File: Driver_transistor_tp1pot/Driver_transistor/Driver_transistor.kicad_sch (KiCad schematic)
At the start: 22 parts, among them J1 Conn_01x01, J2 Conn_01x03, Q1 BC557, Q2 BC548, Q3 BC548, Q4 BU208A

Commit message: actualizacion
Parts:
- added J6: Conn_01x01, Connector_PinHeader_2.00mm:PinHeader_1x01_P2.00mm_Vertical, symbol Connector_Generic:Conn_01x01
- Q4: footprint Package_TO_SOT_THT:TO-220-3_Vertical -> Package_TO_SOT_THT:TO-3
- R8: footprint Resistor_THT:R_Axial_DIN0207_L6.3mm_D2.5mm_P7.62mm_Horizontal -> Resistor_THT:R_Axial_Power_L20.0mm_W6.4mm_P22.40mm
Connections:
- net GND: now also Q4.1 (E), J6.1 (Pin_1); no longer Q4.3 (E)
- net at JP1.2 (B), R8.2: now also Q4.3 (C); no longer Q4.2 (C)
- net at D3.1 (K), JP2.2 (B): now also Q4.2 (B); no longer Q4.1 (B)
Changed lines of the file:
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@@
+    (stroke (width 0) (type default))
+  )
+  (wire (pts (xy 81.28 48.26) (xy 77.47 48.26))
+    (stroke (width 0) (type default))
+  )
+  (wire (pts (xy 77.47 48.26) (xy 77.47 50.8))
     (stroke (width 0) (type default))
   )
@@
     )
   )
+  (symbol (lib_id "Connector_Generic:Conn_01x01") (at 86.36 48.26 0) (unit 1)
+    (in_bom yes) (on_board yes) (dnp no) (fields_autoplaced)
+    (property "Reference" "J6" (at 88.9 47.625 0)
+      (effects (font (size 1.27 1.27)) (justify left))
+    )
+    (property "Value" "Conn_01x01" (at 88.9 50.165 0)
+      (effects (font (size 1.27 1.27)) (justify left))
+    )
+    (property "Footprint" "Connector_PinHeader_2.00mm:PinHeader_1x01_P2.00mm_Vertical" (at 86.36 48.26 0)
+      (effects (font (size 1.27 1.27)) hide)
+    )
+    (property "Datasheet" "~" (at 86.36 48.26 0)
+      (effects (font (size 1.27 1.27)) hide)
+    )
+    (pin "1")
+    (instances
+      (project "Driver_transistor"
+        (path "/e4287a4b-c4f2-447b-b63a-9e2c3468b7f7"
+          (reference "J6") (unit 1)
+        )
+      )
+    )
+  )
   (symbol (lib_id "Transistor_BJT:BUT11") (at 214.63 86.36 0) (unit 1)
     (in_bom yes) (on_board yes) (dnp no) (fields_autoplaced)
@@
       (effects (font (size 1.27 1.27)) (justify left))
     )
-    (property "Footprint" "Package_TO_SOT_THT:TO-220-3_Vertical" (at 219.71 88.265 0)
+    (property "Footprint" "Package_TO_SOT_THT:TO-3" (at 219.71 88.265 0)
       (effects (font (size 1.27 1.27) italic) (justify left) hide)
     )
@@
       (effects (font (size 1.27 1.27)) (justify left))
     )
-    (property "Footprint" "Resistor_THT:R_Axial_DIN0207_L6.3mm_D2.5mm_P7.62mm_Horizontal" (at 215.392 66.04 90)
+    (property "Footprint" "Resistor_THT:R_Axial_Power_L20.0mm_W6.4mm_P22.40mm" (at 215.392 66.04 90)
       (effects (font (size 1.27 1.27)) hide)
     )
@@
         )
       )
+    )
+  )
+  (symbol (lib_id "power:GND") (at 77.47 50.8 0) (unit 1)
+    (in_bom yes) (on_board yes) (dnp no) (fields_autoplaced)
+    (property "Reference" "#PWR019" (at 77.47 57.15 0)
+      (effects (font (size 1.27 1.27)) hide)
+    )
+    (property "Value" "GND" (at 77.47 55.88 0)
+      (effects (font (size 1.27 1.27)))
+    )
+    (property "Footprint" "" (at 77.47 50.8 0)
+      (effects (font (size 1.27 1.27)) hide)
+    )
+    (property "Datasheet" "" (at 77.47 50.8 0)
+      (effects (font (size 1.27 1.27)) hide)
+    )
+    (pin "1")
+    (instances
+      (project "Driver_transistor"
+        (path "/e4287a4b-c4f2-447b-b63a-9e2c3468b7f7"
+          (reference "#PWR019") (unit 1)
+        )
+      )

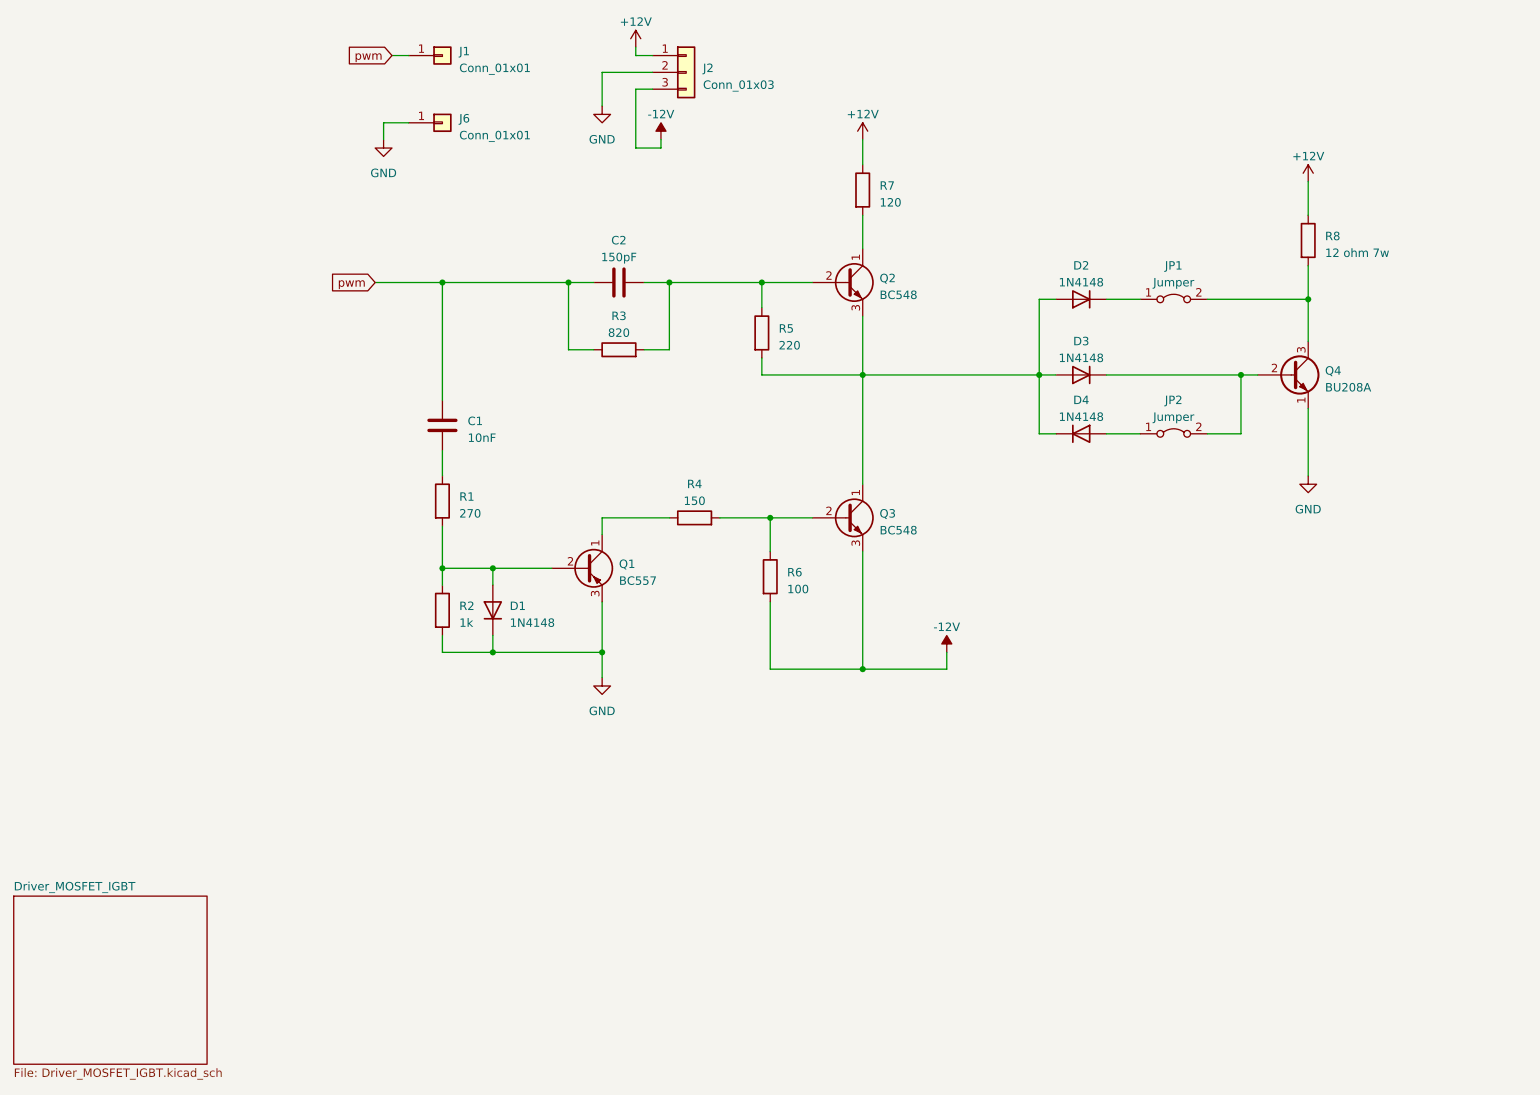
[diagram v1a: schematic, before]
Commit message: rediseño driver BJT
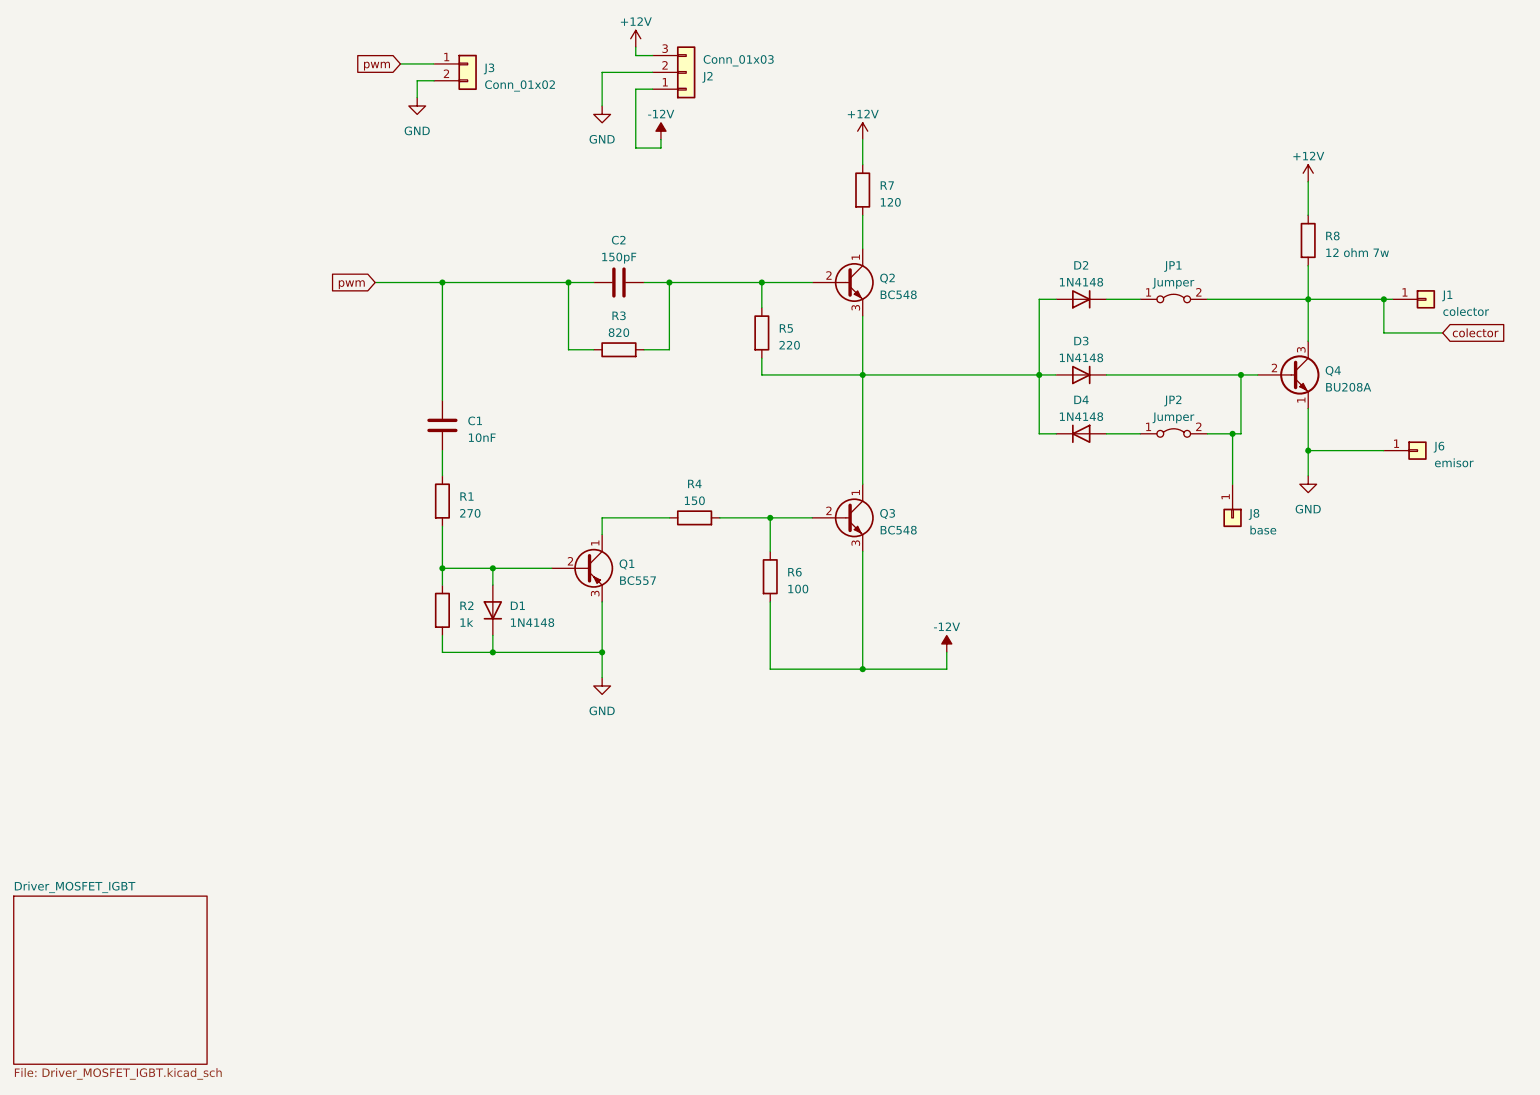
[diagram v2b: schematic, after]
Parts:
- added J3: Conn_01x02, TerminalBlock_Altech:Altech_AK300_1x02_P5.00mm_45-Degree, symbol Connector_Generic:Conn_01x02
- added J8: base, Connector_PinHeader_2.00mm:PinHeader_1x01_P2.00mm_Vertical, symbol Connector_Generic:Conn_01x01
- J1: value Conn_01x01 -> colector
- J2: footprint Connector_Wire:SolderWire-0.25sqmm_1x03_P4.2mm_D0.65mm_OD1.7mm -> TerminalBlock_Altech:Altech_AK300_1x03_P5.00mm_45-Degree
- J6: value Conn_01x01 -> emisor
- R7: footprint Resistor_THT:R_Axial_DIN0207_L6.3mm_D2.5mm_P7.62mm_Horizontal -> Resistor_THT:R_Axial_DIN0207_L6.3mm_D2.5mm_P15.24mm_Horizontal
- R8: footprint Resistor_THT:R_Axial_Power_L20.0mm_W6.4mm_P22.40mm -> Resistor_THT:R_Axial_Power_L20.0mm_W6.4mm_P30.48mm
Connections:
- net +12V: now also J2.3 (Pin_3); no longer J2.1 (Pin_1)
- net -12V: now also J2.1 (Pin_1); no longer J2.3 (Pin_3)
- net GND: now also J3.2 (Pin_2)
- net pwm: now also J3.1 (Pin_1); no longer J1.1 (Pin_1)
- net colector: now reaches JP1.2 (B), Q4.3 (C), R8.2
- net colector: now also J1.1 (Pin_1)
- net at D3.1 (K), JP2.2 (B), Q4.2 (B): now also J8.1 (Pin_1)
